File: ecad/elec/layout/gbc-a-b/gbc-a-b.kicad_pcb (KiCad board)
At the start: 2 copper layers, 225.7 x 100.8 mm, 0 parts

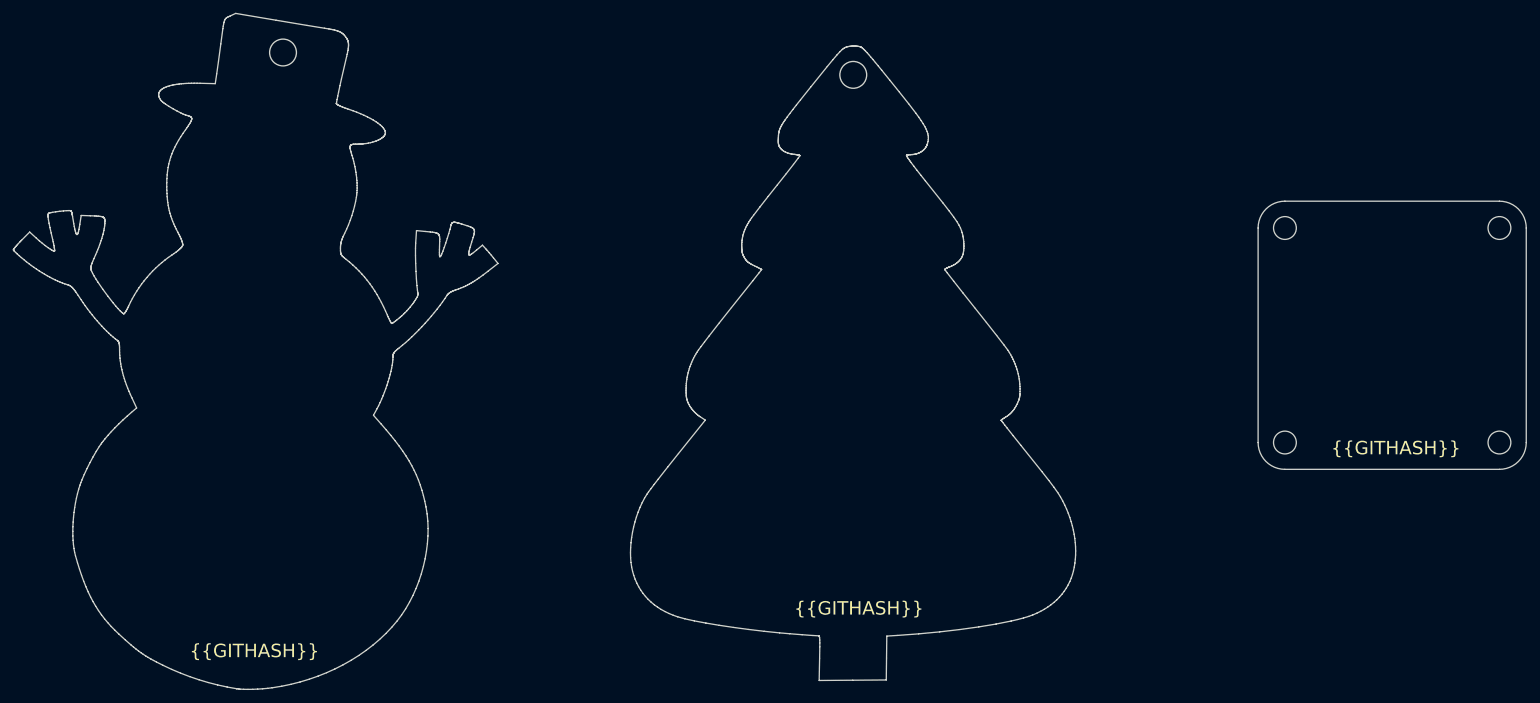
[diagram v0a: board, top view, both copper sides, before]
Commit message: WIP fleshing out and redoing some of the design to add some footprints / components for slik / membranes / etc.
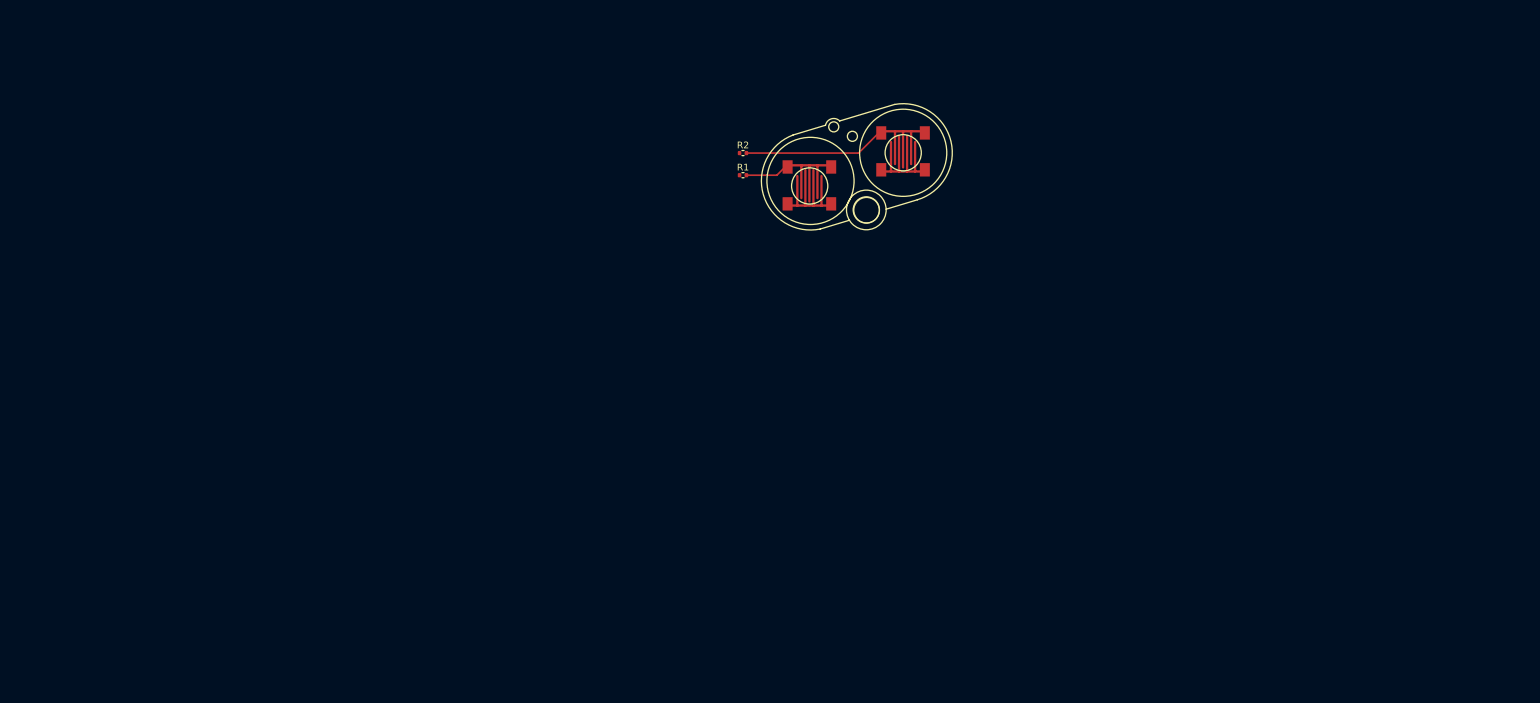
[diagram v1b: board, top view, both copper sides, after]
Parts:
- added R1: 62.5mW Thick Film Resistors 50V ±100ppm/℃ ±1% 10kΩ 0402 Chi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, lib:R0402, F.Cu at (144.8, 73.9)
- added R2: 62.5mW Thick Film Resistors 50V ±100ppm/℃ ±1% 10kΩ 0402 Chi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, lib:R0402, F.Cu at (144.8, 70.6)
- added U1: , lib:GAMEBOY_COLOR_A_B_BUTTON_MEMBRANE, F.Cu at (161.7, 73.0)
- added U2: , lib:GBC_A_B_BUTTON, F.Cu at (154.7, 75.4)
- added U3: , lib:GBC_A_B_BUTTON, F.Cu at (168.7, 70.4)
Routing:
- net b: track 0.00 -> 21.0 mm
- net a: track 0.00 -> 6.28 mm
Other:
- board outline removed
- board text removed: "{{GITHASH}}"
